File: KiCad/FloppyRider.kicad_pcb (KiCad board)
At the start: 2 copper layers, 88.9 x 59.7 mm, 25 parts, among them J1 PC disk controller interface, J2 IBM Diskette Host power, J3 IBM 51TD Diskette unit, J4 Alternative power connector, SW1 Reset, U1 74LS08, U2 74LS02, U3 74LS06, U4 74LS74

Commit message: Changes for initial release
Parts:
- added R11: 1K, Resistor_SMD:R_0603_1608Metric, F.Cu at (118.1, 94.0)
- added R8: 1K, Resistor_SMD:R_0603_1608Metric, F.Cu at (118.1, 86.4)
- added R9: 1K, Resistor_SMD:R_0603_1608Metric, F.Cu at (118.1, 88.9)
- R10, R5, R6, R7: value 4,7K -> 1K
- moved R10 38.7 mm to (118.1, 91.4)
- moved R1 25.4 mm to (118.1, 66.0)
- moved R4 10.2 mm to (118.1, 76.2)
- moved R6 7.63 mm to (118.1, 81.3)
- moved R3 5.15 mm to (118.1, 71.1)
- moved U1 3.59 mm to (97.8, 97.8), turned to 90 degrees
- moved U4 2.84 mm to (110.5, 97.8), turned to 270 degrees
- moved R2 2.67 mm to (118.1, 68.6)
- moved R7 2.58 mm to (118.1, 83.8)
- moved R13 0.83 mm to (118.1, 73.7)
- moved R5 0.83 mm to (118.1, 78.7)
- renumbered R9 to R12, R8 to R13
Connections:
- R1 pad 2: /index -> /disk_chng_rdy
- R10 pad 2: /step -> /drive_b
- R2 pad 2: /read_data -> /head_1_select
- R3 pad 2: /track_0 -> /read_data
- R4 pad 2: /disk_chng_rdy -> /track_0
- R6 pad 2: /motor_b -> /write_data
- R7 pad 2: /drive_b -> /step
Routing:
- net /8_head_engage: track 71.4 -> 51.5 mm
- net /step: track 74.9 -> 55.5 mm
- net /drive_b: track 90.3 -> 109.3 mm
- net /write_protected: track 20.6 -> 36.6 mm
- net VCC: track 173.6 -> 157.7 mm
- net /8_index: track 47.3 -> 33.1 mm
- net /+24V: track 62.1 -> 49.1 mm
- net /8_write_erase_gate: track 84.8 -> 72.9 mm, vias 3 -> 1
- net Net-(U1-Pad8): track 22.8 -> 11.0 mm
- net /read_data: track 48.8 -> 38.4 mm
- net Net-(U1-Pad6): track 30.3 -> 22.3 mm, vias 2 -> 0
- net /disk_chng_rdy: track 42.6 -> 35.3 mm
- net /track_0_neg: track 25.1 -> 18.2 mm, vias 1 -> 0
- net GND: track 277.5 -> 270.8 mm, vias 1 -> 0
- net /drive_b_neg: track 40.9 -> 47.2 mm, vias 2 -> 0
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
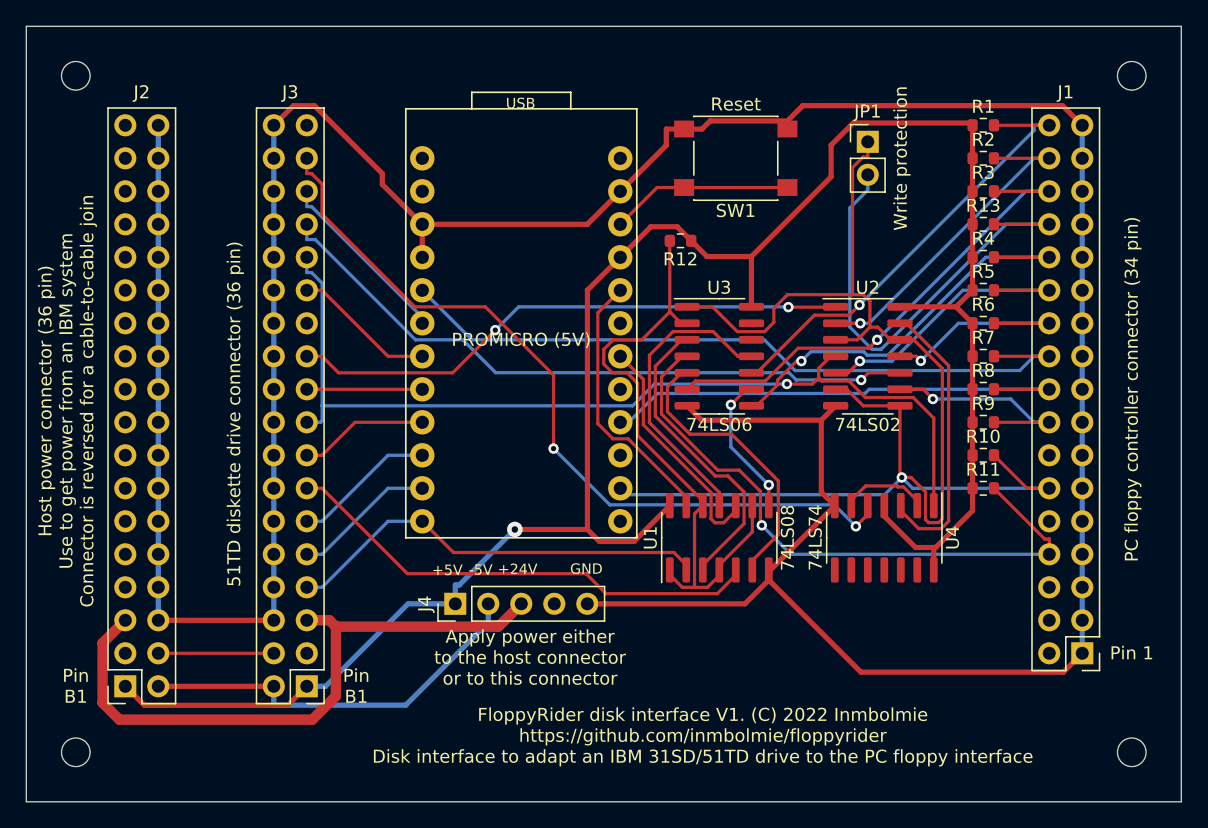
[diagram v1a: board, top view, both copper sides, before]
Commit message: Added transistor to drive write/erase gate signals
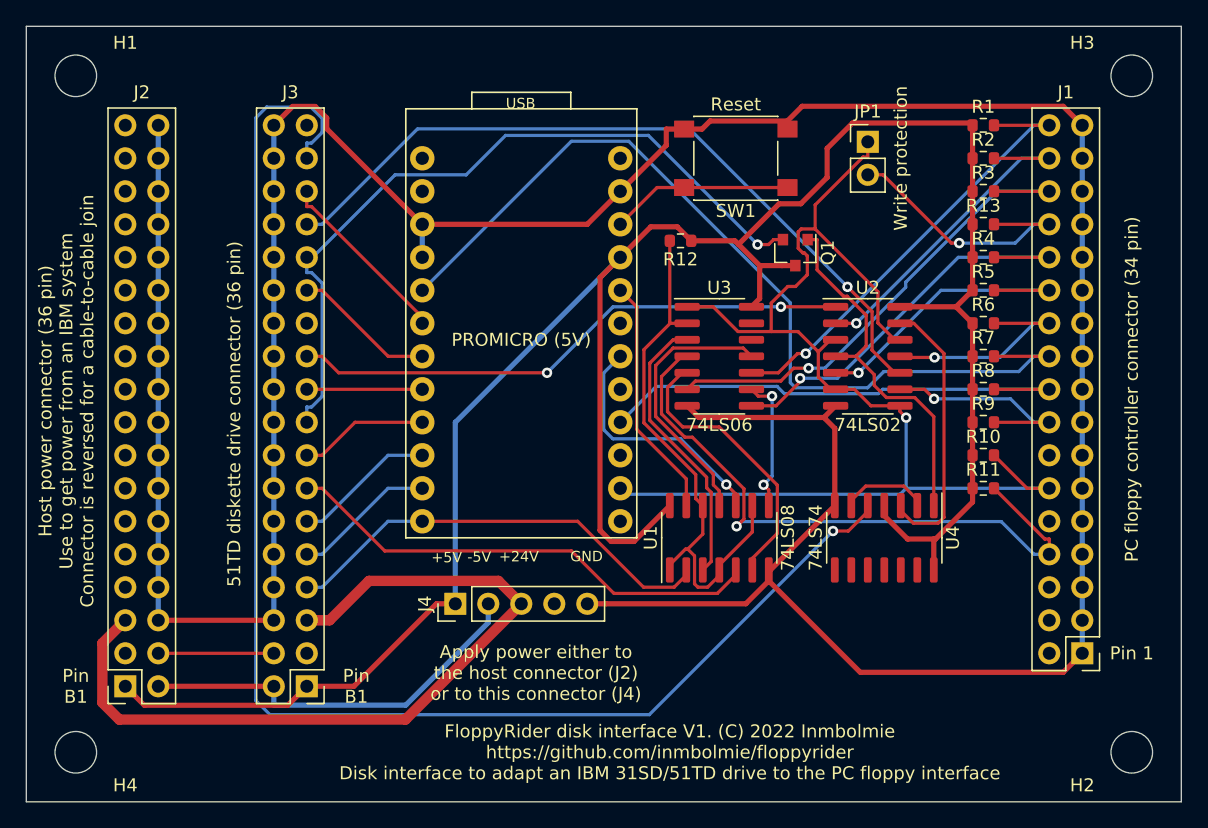
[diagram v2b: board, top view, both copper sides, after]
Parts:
- added Q1: SS8050, Package_TO_SOT_SMD:SOT-23, F.Cu at (103.6, 75.8)
- H1, H2, H3, H4: footprint MountingHole:MountingHole_2.2mm_M2 -> MountingHole:MountingHole_3.2mm_M3
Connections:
- U2 pad 4: /8_write_erase_gate -> /write_erase_gate
- U4 pad 1: /8_write_erase_gate -> /write_erase_gate
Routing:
- net /8_write_data: track 61.3 -> 108.9 mm, vias 2 -> 1
- net /write_erase_gate: track 0.00 -> 28.6 mm
- net VCC: track 157.7 -> 178.3 mm, vias 1 -> 0
- net /write_protected: track 36.6 -> 21.0 mm, vias 0 -> 1
- net /8_write_erase_gate: track 72.9 -> 58.5 mm
- net /step: track 55.5 -> 69.7 mm
- net /+24V: track 49.1 -> 62.0 mm
- net /drive_b: track 109.3 -> 98.6 mm
- net /8_head_engage: track 51.5 -> 58.2 mm
- net /drive_b_neg: track 47.2 -> 42.2 mm
- net Net-(U1-Pad11): track 23.2 -> 21.0 mm
- net /disk_chng_rdy_neg: track 20.8 -> 18.7 mm
- net Net-(U1-Pad3): track 23.7 -> 21.8 mm
- net /index: track 48.3 -> 49.7 mm
- net /8_index: track 33.1 -> 34.2 mm
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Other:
- board text added: "Apply power either to the host connector (J2) or to this connector (J4)"
- board text removed: "Apply power either to the host connector or to this connector"

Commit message: Added hard write protection switch
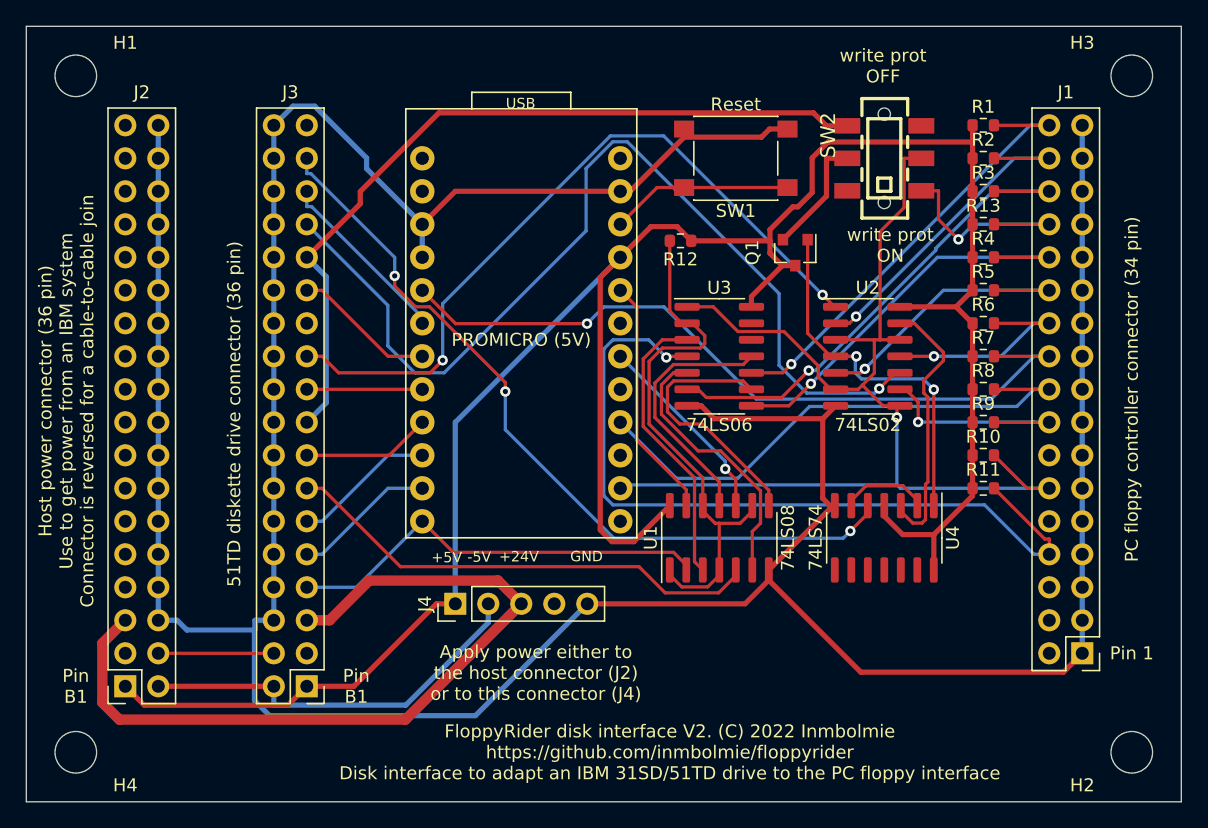
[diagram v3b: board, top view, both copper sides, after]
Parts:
- removed JP1: Write protection, Connector_PinHeader_2.54mm:PinHeader_1x02_P2.54mm_Vertical
- added SW2: Write prot, dpdt_2:SW-TH_K3-2235S-K1, F.Cu at (110.5, 68.6)
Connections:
- Q1 pad 2: /8_write_erase_gate -> /write_erase_gate_prot
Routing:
- net /8_write_data: track 108.9 -> 60.8 mm, vias 1 -> 3
- net /8_head_engage: track 58.2 -> 74.3 mm
- net /8_select_head: track 43.3 -> 56.8 mm
- net /index: track 49.7 -> 61.8 mm
- net GND: track 270.7 -> 282.1 mm
- net /step: track 69.7 -> 58.4 mm, vias 0 -> 1
- net Net-(U1-Pad8): track 10.7 -> 20.3 mm, vias 2 -> 0
- net /write_erase_gate_prot: track 0.00 -> 9.25 mm
- net /drive_b: track 98.6 -> 89.8 mm
- net /track_0_neg: track 19.3 -> 15.2 mm
- net /write_protected: track 21.0 -> 17.4 mm
- net /direction: track 38.8 -> 41.9 mm
- net /8_write_erase_gate: track 58.5 -> 61.1 mm, vias 1 -> 0
- net VCC: track 178.3 -> 176.9 mm
- net Net-(U1-Pad11): track 21.0 -> 19.8 mm
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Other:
- board text added: "FloppyRider disk interface V2. (C) 2022 Inmbolmie https://github.com/inmbolmie/floppyrider Disk interface to adapt an IBM 31SD/51TD drive to the PC floppy interface"
- board text added: "write prot OFF"
- board text added: "write prot ON"
- board text removed: "FloppyRider disk interface V1. (C) 2022 Inmbolmie https://github.com/inmbolmie/floppyrider Disk interface to adapt an IBM 31SD/51TD drive to the PC floppy interface"
